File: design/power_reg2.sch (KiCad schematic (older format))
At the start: 7 parts, among them U2 MIC2954

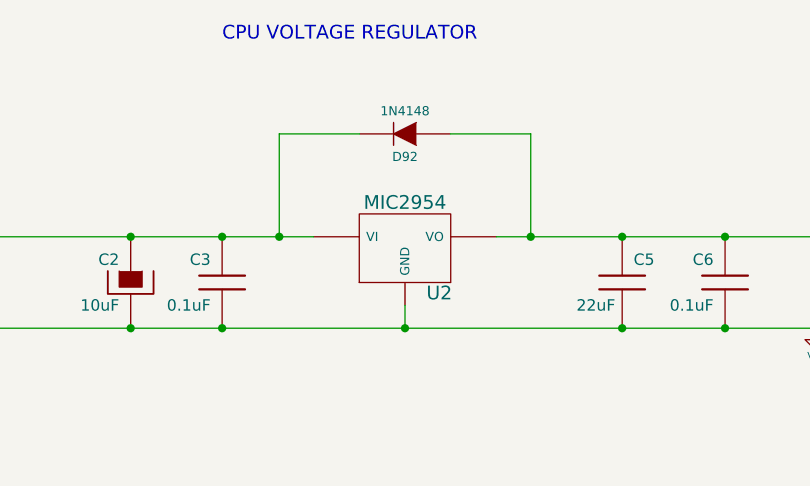
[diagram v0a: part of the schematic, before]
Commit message: Changed cpu regulator, updated BOM
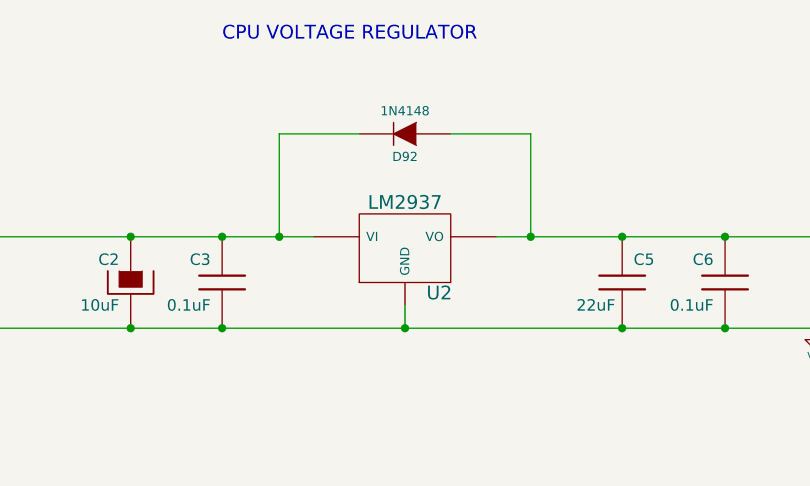
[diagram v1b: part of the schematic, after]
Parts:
- U2: value MIC2954 -> LM2937; Field2 576-1154-1-ND -> LM2937IMP-5.0CT-ND
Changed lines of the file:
@@
-EESchema Schematic File Version 2  date Sat 22 Jan 2011 04:28:46 PM ART
+EESchema Schematic File Version 2  date Fri 28 Jan 2011 01:02:03 AM ART
 LIBS:power
 LIBS:freeEMS_lib
@@
 Sheet 33 56
 Title "Puma board"
-Date "22 jan 2011"
+Date "28 jan 2011"
 Rev "A.07"
 Comp "diyefi.org"
@@
 P 6050 3350
 F 0 "U2" H 6200 3154 60  0000 C CNN
-F 1 "MIC2954" H 6050 3550 60  0000 C CNN
-F 5 "576-1154-1-ND" H 6050 3350 60  0001 C CNN "Field2"
+F 1 "LM2937" H 6050 3550 60  0000 C CNN
+F 5 "LM2937IMP-5.0CT-ND" H 6050 3350 60  0001 C CNN "Field2"
 	1    6050 3350
 	1    0    0    -1

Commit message: updating bom, lets commit this before I run a script to update the footprints for the resistors
Signed-off-by: Jared Harvey <TortiseGIT@jaredharvey.com>
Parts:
- C5: footprint C1V7 -> SM2512
- D1: footprint D4-SMB -> SOD-123; Field1 newark,18C8923 -> (none); Field2 1N4448W-FDICT-ND -> (none); Field3 DIGI,1N4007RLOSCT-ND -> (none); Field4 vendor2, smd w hem -> (none); Field5 max,V -> (none); Field6 x,x -> (none); Field7 construct -> -; Field8 other,more,stuff -> -; mfg (none) -> Diodes Inc; mfg# (none) -> 1N4448W-7-F; vend1 (none) -> digikey; vend1# (none) -> 1N4448W-FDICT-ND; vend2 (none) -> -; vend2# (none) -> -
- D92: footprint (none) -> SOD-123
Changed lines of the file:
@@
-EESchema Schematic File Version 2  date 2/13/2011 11:33:14 AM
+EESchema Schematic File Version 2  date 2/16/2011 5:39:15 AM
 LIBS:power
 LIBS:freeEMS_lib
@@
 Sheet 33 56
 Title "Puma board"
-Date "13 feb 2011"
+Date "16 feb 2011"
 Rev "v0.02"
 Comp "diyefi.org"
@@
 F 0 "C5" H 7050 3600 50  0000 L CNN
 F 1 "22uF" H 6800 3400 50  0000 L CNN
-F 2 "C1V7" V 1130 2600 60  0001 C CNN
+F 2 "SM2512" V 1130 2600 60  0001 C CNN
 F 4 "AVX" V 1130 2600 60  0001 C CNN "mfg"
 F 5 "TAJC226M016RNJ" V 1130 2600 60  0001 C CNN "mfg#"
@@
 F 0 "D92" H 6050 2950 40  0000 C CNN
 F 1 "1N4148" H 6050 2750 40  0000 C CNN
+F 2 "SOD-123" H 6050 2850 60  0001 C CNN
 F 4 "Micro Commercial Co" V 1130 2600 60  0001 C CNN "mfg"
 F 5 "1N4148W-TP" V 1130 2600 60  0001 C CNN "mfg#"
@@
 F 0 "D1" H 2850 3400 40  0000 C CNN
 F 1 "1N4448" H 2850 3200 40  0000 C CNN
-F 2 "D4-SMB" H 2950 3500 60  0001 C CNN
-F 4 "newark,18C8923" H 2950 3500 60  0001 C CNN "Field1"
-F 5 "1N4448W-FDICT-ND" H 2950 3500 60  0001 C CNN "Field2"
-F 6 "DIGI,1N4007RLOSCT-ND" H -3270 2600 60  0001 C CNN "Field3"
-F 7 "vendor2, smd w hem" H -3270 2600 60  0001 C CNN "Field4"
-F 8 "max,V" H -3270 2600 60  0001 C CNN "Field5"
-F 9 "x,x" H -3270 2600 60  0001 C CNN "Field6"
-F 10 "construct" H -3270 2600 60  0001 C CNN "Field7"
-F 11 "other,more,stuff" H -3270 2600 60  0001 C CNN "Field8"
+F 2 "SOD-123" H 2950 3500 60  0001 C CNN
+F 4 "Diodes Inc" H 2950 3500 60  0001 C CNN "mfg"
+F 5 "1N4448W-7-F" H 2950 3500 60  0001 C CNN "mfg#"
+F 6 "digikey" H -3270 2600 60  0001 C CNN "vend1"
+F 7 "1N4448W-FDICT-ND" H -3270 2600 60  0001 C CNN "vend1#"
+F 8 "-" H -3270 2600 60  0001 C CNN "vend2"
+F 9 "-" H -3270 2600 60  0001 C CNN "vend2#"
+F 10 "-" H -3270 2600 60  0001 C CNN "Field7"
+F 11 "-" H -3270 2600 60  0001 C CNN "Field8"
 	1    2850 3300
 	1    0    0    1

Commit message: Schematic BOM is now fully populated with only 3 exceptions, .cmp file is obsolete at this point, so it has been removed.
Signed-off-by: Jared Harvey <TortiseGIT@jaredharvey.com>
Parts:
- C2: footprint C8 -> C1V7
- U2: footprint (none) -> SOT223; Field2 LM2937IMP-5.0CT-ND -> (none); mfg (none) -> national semi; mfg# (none) -> LM2937IMP-5.0/NOPB; vend1 (none) -> digikey; vend1# (none) -> LM2937IMP-5.0CT-ND
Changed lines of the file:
@@
-EESchema Schematic File Version 2  date 2/16/2011 5:39:15 AM
+EESchema Schematic File Version 2  date 2/16/2011 8:44:20 AM
 LIBS:power
 LIBS:freeEMS_lib
@@
 F 0 "U2" H 6200 3154 60  0000 C CNN
 F 1 "LM2937" H 6050 3550 60  0000 C CNN
-F 5 "LM2937IMP-5.0CT-ND" H 6050 3350 60  0001 C CNN "Field2"
+F 2 "SOT223" H 6050 3350 60  0001 C CNN
+F 4 "national semi" H 6050 3350 60  0001 C CNN "mfg"
+F 5 "LM2937IMP-5.0/NOPB" H 6050 3350 60  0001 C CNN "mfg#"
+F 6 "digikey" H 6050 3350 60  0001 C CNN "vend1"
+F 7 "LM2937IMP-5.0CT-ND" H 6050 3350 60  0001 C CNN "vend1#"
 	1    6050 3350
 	1    0    0    -1
 $EndComp
 $Comp
-L VSS #PWR069
+L VSS #PWR067
 U 1 1 4C2F52A0
 P 7850 3750
-F 0 "#PWR069" H 7850 3750 30  0001 C CNN
+F 0 "#PWR067" H 7850 3750 30  0001 C CNN
 F 1 "VSS" H 7850 3680 30  0000 C CNN
 	1    7850 3750
@@
 F 0 "C2" H 4900 3600 50  0000 L CNN
 F 1 "10uF" H 4900 3400 50  0000 L CNN
-F 2 "C8" V 1130 2600 60  0001 C CNN
+F 2 "C1V7" V 1130 2600 60  0001 C CNN
 F 4 "Nichicon" V 1130 2600 60  0001 C CNN "mfg"
 F 5 "UVZ1C100MDD" V 1130 2600 60  0001 C CNN "mfg#"
@@
 $EndComp
 $Comp
-L GND #PWR070
+L GND #PWR068
 U 1 1 486CA86E
 P 2600 3750
-F 0 "#PWR070" H 2600 3750 30  0001 C CNN
+F 0 "#PWR068" H 2600 3750 30  0001 C CNN
 F 1 "GND" H 2600 3680 30  0001 C CNN
 	1    2600 3750
